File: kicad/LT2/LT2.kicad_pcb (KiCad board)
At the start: 2 copper layers, 23 parts

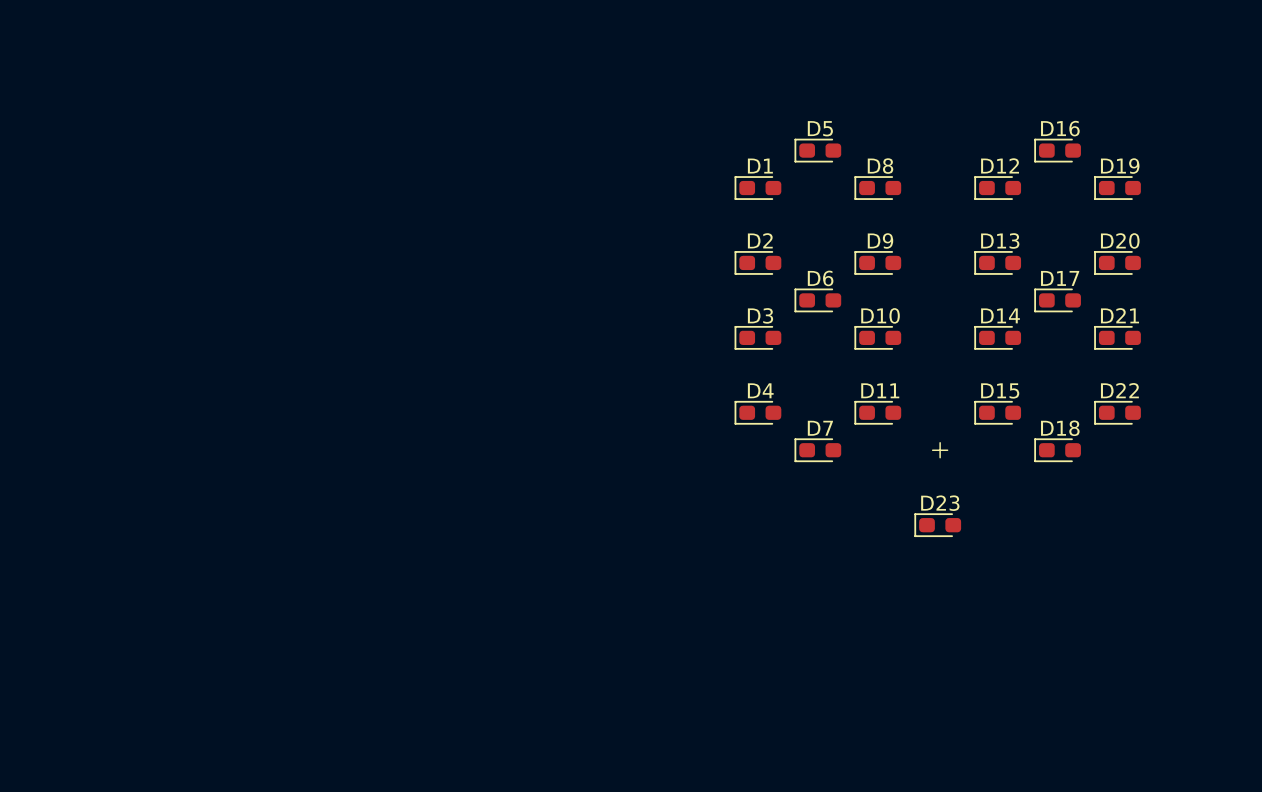
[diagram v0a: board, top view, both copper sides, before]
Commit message: placing battey + rot encoder
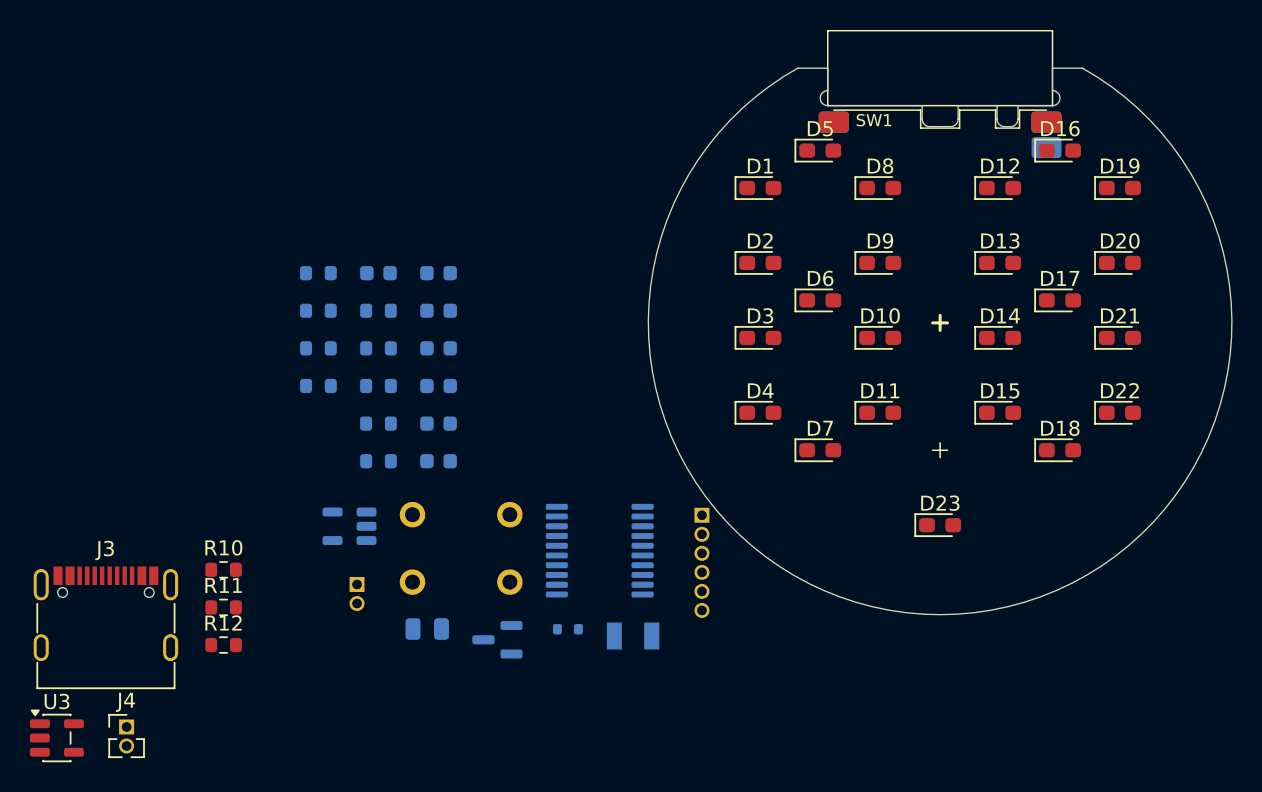
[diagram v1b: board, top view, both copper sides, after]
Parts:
- added C1: 10uF, Capacitor_SMD:C_0805_2012Metric, B.Cu at (115.8, 111.9)
- added C2: 100nF, Capacitor_SMD:C_0603_1608Metric, B.Cu at (116.5, 88.2)
- added C3: 12pF, Capacitor_SMD:C_0603_1608Metric, B.Cu at (116.5, 90.7)
- added C4: 12pF, Capacitor_SMD:C_0603_1608Metric, B.Cu at (116.5, 93.2)
- added C5: 1nF, Capacitor_SMD:C_0603_1608Metric, B.Cu at (116.5, 95.7)
- added C6: 1nF, Capacitor_SMD:C_0603_1608Metric, B.Cu at (116.5, 98.2)
- added C7: 1nF, Capacitor_SMD:C_0603_1608Metric, B.Cu at (116.5, 100.7)
- added C8: 1nF, Capacitor_SMD:C_0603_1608Metric, B.Cu at (112.5, 88.2)
- added D24: 1N914WT, Diode_SMD:D_SOD-523, B.Cu at (125.2, 112.0)
- added J1: Conn_01x06_Socket, Connector_PinHeader_1.27mm:PinHeader_1x06_P1.27mm_Vertical, B.Cu at (134.1, 104.3)
- added J2: Conn_01x02_Socket, Connector_PinHeader_1.27mm:PinHeader_1x02_P1.27mm_Vertical, B.Cu at (111.1, 109.0)
- added J3: USB_C_Receptacle_USB2.0_16P, Connector_USB:USB_C_Receptacle_G-Switch_GT-USB-7010ASV, F.Cu at (94.3, 112.1)
- added J4: Conn_01x02_Socket, Connector_PinHeader_1.27mm:PinHeader_1x02_P1.27mm_Vertical, F.Cu at (95.7, 118.5)
- added Q1: 2N7002, Package_TO_SOT_SMD:SOT-23, B.Cu at (120.5, 112.7)
- added R1: 470R, Resistor_SMD:R_0603_1608Metric, B.Cu at (112.5, 90.7)
- added R10: 10k, Resistor_SMD:R_0603_1608Metric, F.Cu at (102.2, 108.0)
- added R11: 5k1, Resistor_SMD:R_0603_1608Metric, F.Cu at (102.2, 110.5)
- added R12: 5k1, Resistor_SMD:R_0603_1608Metric, F.Cu at (102.2, 113.0)
- added R2: 470R, Resistor_SMD:R_0603_1608Metric, B.Cu at (112.5, 93.2)
- added R3: 470R, Resistor_SMD:R_0603_1608Metric, B.Cu at (112.5, 95.7)
- added R4: 470R, Resistor_SMD:R_0603_1608Metric, B.Cu at (112.5, 98.2)
- added R5: 470R, Resistor_SMD:R_0603_1608Metric, B.Cu at (112.5, 100.7)
- added R6: 470R, Resistor_SMD:R_0603_1608Metric, B.Cu at (108.5, 88.2)
- added R7: 100k, Resistor_SMD:R_0603_1608Metric, B.Cu at (108.5, 90.7)
- added R8: 100k, Resistor_SMD:R_0603_1608Metric, B.Cu at (108.5, 93.2)
- added R9: 100k, Resistor_SMD:R_0603_1608Metric, B.Cu at (108.5, 95.7)
- added SW1: RotaryEncoder_Switch, LT2:rotary_encoder_PEC11S-929K, F.Cu at (150.0, 77.0)
- added SW2: SW_Push, Button_Switch_THT:SW_TH_Tactile_Omron_B3F-100x, B.Cu at (121.3, 104.3)
- added U1: STM32L031F6Px, Package_SO:TSSOP-20_4.4x6.5mm_P0.65mm, B.Cu at (127.3, 106.7)
- added U2: MCP1711-300/OT_SOT23-5, Package_TO_SOT_SMD:SOT-23-5, B.Cu at (110.6, 105.1)
- added U3: MCP73812T-420I-OT, Package_TO_SOT_SMD:SOT-23-5, F.Cu at (91.1, 119.2)
- added Y1: 32kHz, Crystal:Crystal_SMD_3215-2Pin_3.2x1.5mm, B.Cu at (129.5, 112.4)
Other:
- board outline added: 38.9 x 36.5 mm
- board text added: "Akku 17 x 34 x 4 mm"

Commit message: some routing
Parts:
- J3, J4, R10, R11, R12, U3: moved to B.Cu
- moved U3 68.3 mm to (157.5, 103.5), turned to 180 degrees
- moved J4 64.9 mm to (159.5, 106.5), turned to 90 degrees
- moved J3 55.9 mm to (150.0, 107.5), turned to 180 degrees
- moved R10 53.8 mm to (155.5, 101.0)
- moved R7 53.2 mm to (161.0, 82.0), turned to 90 degrees
- moved R8 52.2 mm to (159.5, 82.0), turned to 90 degrees
- moved R12 51.7 mm to (152.5, 101.0), turned to 180 degrees
- moved U2 51.4 mm to (162.0, 103.5), turned to 0 degrees
- moved C7 49.5 mm to (161.0, 79.0), turned to -90 degrees
- moved C1 49.1 mm to (163.5, 100.5)
- moved C6 47.1 mm to (159.5, 79.0), turned to -90 degrees
- moved R11 46.3 mm to (147.5, 101.0)
- moved R1 44.1 mm to (156.5, 94.5), turned to 0 degrees
- moved C5 41.8 mm to (158.1, 91.0), turned to 0 degrees
- moved C4 41.7 mm to (158.1, 89.5)
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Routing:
- net Net-(D14-K): track 0.00 -> 85.3 mm, vias 0 -> 3
- net Net-(D13-K): track 0.00 -> 69.1 mm, vias 0 -> 4
- net Net-(D1-A): track 0.00 -> 62.9 mm, vias 0 -> 4
- net Net-(D1-K): track 0.00 -> 59.7 mm, vias 0 -> 1
- net Net-(D11-A): track 0.00 -> 52.7 mm, vias 0 -> 1
- net GND: track 0.00 -> 36.9 mm, vias 0 -> 3
- net VCC: track 0.00 -> 34.2 mm, vias 0 -> 1
- net Net-(D10-K): track 0.00 -> 30.9 mm, vias 0 -> 4
- net RST: track 0.00 -> 16.6 mm
- net Net-(U3-CE): track 0.00 -> 16.3 mm
- net LPUART_TX: track 0.00 -> 16.1 mm
- net VIBRA: track 0.00 -> 14.2 mm
- net +BATT: track 0.00 -> 10.1 mm
- net ENC_A: track 0.00 -> 8.19 mm, vias 0 -> 1
- net ENC_BTN: track 0.00 -> 6.69 mm, vias 0 -> 1
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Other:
- copper layers 2 -> 4
